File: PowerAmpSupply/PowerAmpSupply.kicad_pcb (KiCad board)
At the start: 2 copper layers, 52 parts, among them Q1 GAN3R2-100CBE, Q2 PNP, Q3 GAN3R2-100CBE, Q4 PNP, U1 LM5123-Q1

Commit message: CleanLVSupply reduce -17V switch frequency
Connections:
- net Net-(Q2-C) renamed /SW
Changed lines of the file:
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@@
 	(net 23 "Net-(U1-RT)")
 	(net 24 "/PGOOD")
-	(net 25 "Net-(Q2-C)")
+	(net 25 "/SW")
 	(footprint "Capacitor_SMD:C_0805_2012Metric"
 		(layer "F.Cu")
@@
 			(size 0.24 0.7)
 			(layers "F.Cu" "F.Paste" "F.Mask")
-			(net 25 "Net-(Q2-C)")
+			(net 25 "/SW")
 			(pinfunction "SW")
 			(pintype "passive")
@@
 			(size 1.5 1.5)
 			(layers "F.Cu" "F.Mask")
-			(net 25 "Net-(Q2-C)")
+			(net 25 "/SW")
 			(pinfunction "1")
 			(pintype "passive")
@@
 			(layers "F.Cu" "F.Paste" "F.Mask")
 			(roundrect_rratio 0.25)
-			(net 25 "Net-(Q2-C)")
+			(net 25 "/SW")
 			(pinfunction "S")
 			(pintype "passive")
@@
 			(layers "F.Cu" "F.Paste" "F.Mask")
 			(roundrect_rratio 0.25)
-			(net 25 "Net-(Q2-C)")
+			(net 25 "/SW")
 			(pinfunction "S")
 			(pintype "passive")
@@
 			(layers "F.Cu" "F.Paste" "F.Mask")
 			(roundrect_rratio 0.25)
-			(net 25 "Net-(Q2-C)")
+			(net 25 "/SW")
 			(pinfunction "S")
 			(pintype "passive")
@@
 			(layers "F.Cu" "F.Paste" "F.Mask")
 			(roundrect_rratio 0.25)
-			(net 25 "Net-(Q2-C)")
+			(net 25 "/SW")
 			(pinfunction "S")
 			(pintype "passive")
@@
 			(layers "F.Cu" "F.Paste" "F.Mask")
 			(roundrect_rratio 0.25)
-			(net 25 "Net-(Q2-C)")
+			(net 25 "/SW")
 			(pintype "passive")
 		)
@@
 			(layers "F.Cu" "F.Paste" "F.Mask")
 			(roundrect_rratio 0.25)
-			(net 25 "Net-(Q2-C)")
+			(net 25 "/SW")
 			(pinfunction "D")
 			(pintype "passive")
@@
 			(layers "F.Cu" "F.Paste" "F.Mask")
 			(roundrect_rratio 0.25)
-			(net 25 "Net-(Q2-C)")
+			(net 25 "/SW")
 			(pinfunction "D")
 			(pintype "passive")
@@
 			(layers "F.Cu" "F.Paste" "F.Mask")
 			(roundrect_rratio 0.25)
-			(net 25 "Net-(Q2-C)")
+			(net 25 "/SW")
 			(pinfunction "D")
 			(pintype "passive")
@@
 			(layers "F.Cu" "F.Paste" "F.Mask")
 			(roundrect_rratio 0.25)
-			(net 25 "Net-(Q2-C)")
+			(net 25 "/SW")
 			(pinfunction "2")
 			(pintype "passive")
@@
 			(layers "F.Cu" "F.Paste" "F.Mask")
 			(roundrect_rratio 0.25)
-			(net 25 "Net-(Q2-C)")
+			(net 25 "/SW")
 			(pinfunction "C")
 			(pintype "passive")
@@
 			(layers "F.Cu" "F.Paste" "F.Mask")
 			(roundrect_rratio 0.25)
-			(net 25 "Net-(Q2-C)")
+			(net 25 "/SW")
 			(pinfunction "A")
 			(pintype "passive")
@@
 			(layers "F.Cu" "F.Paste" "F.Mask")
 			(roundrect_rratio 0.25)
-			(net 25 "Net-(Q2-C)")
+			(net 25 "/SW")
 			(pinfunction "A")
 			(pintype "passive")

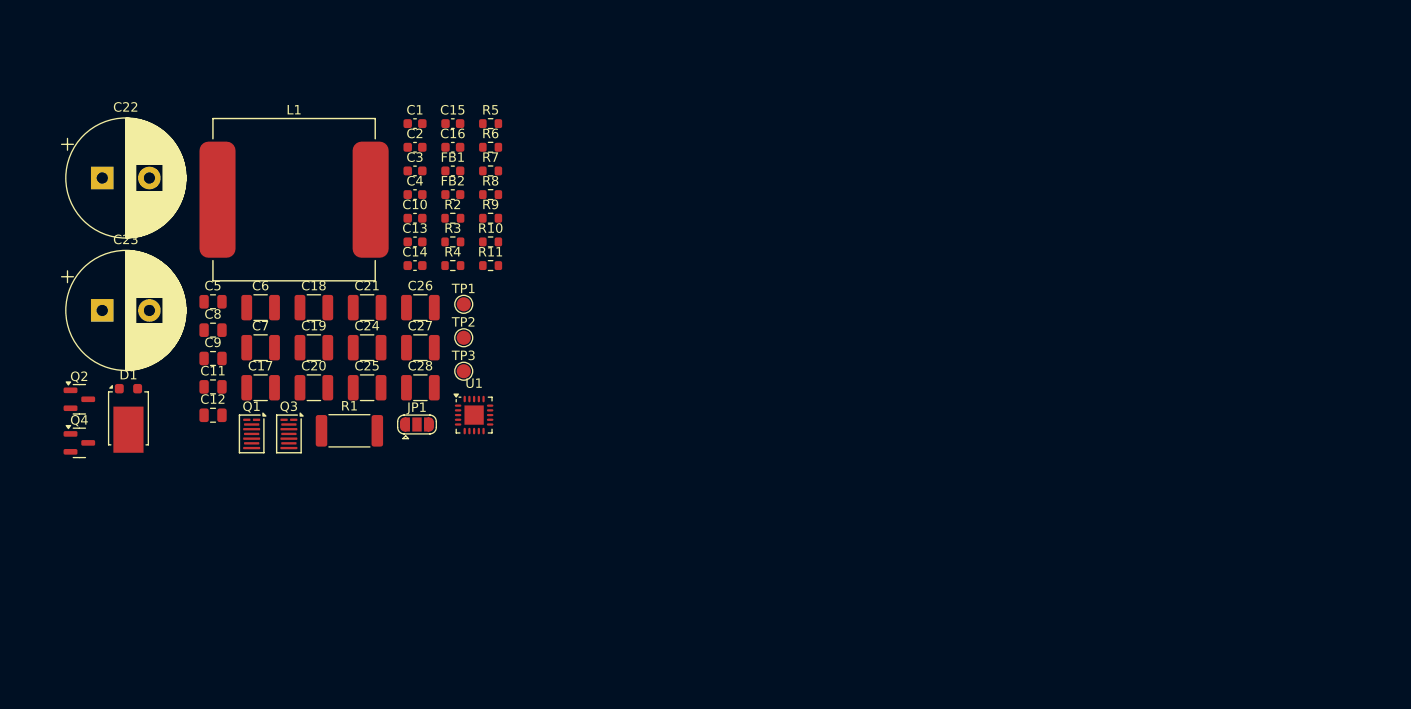
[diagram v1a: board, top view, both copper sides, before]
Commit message: PowerAmplifier initially complete, PowerAmpSupply progress
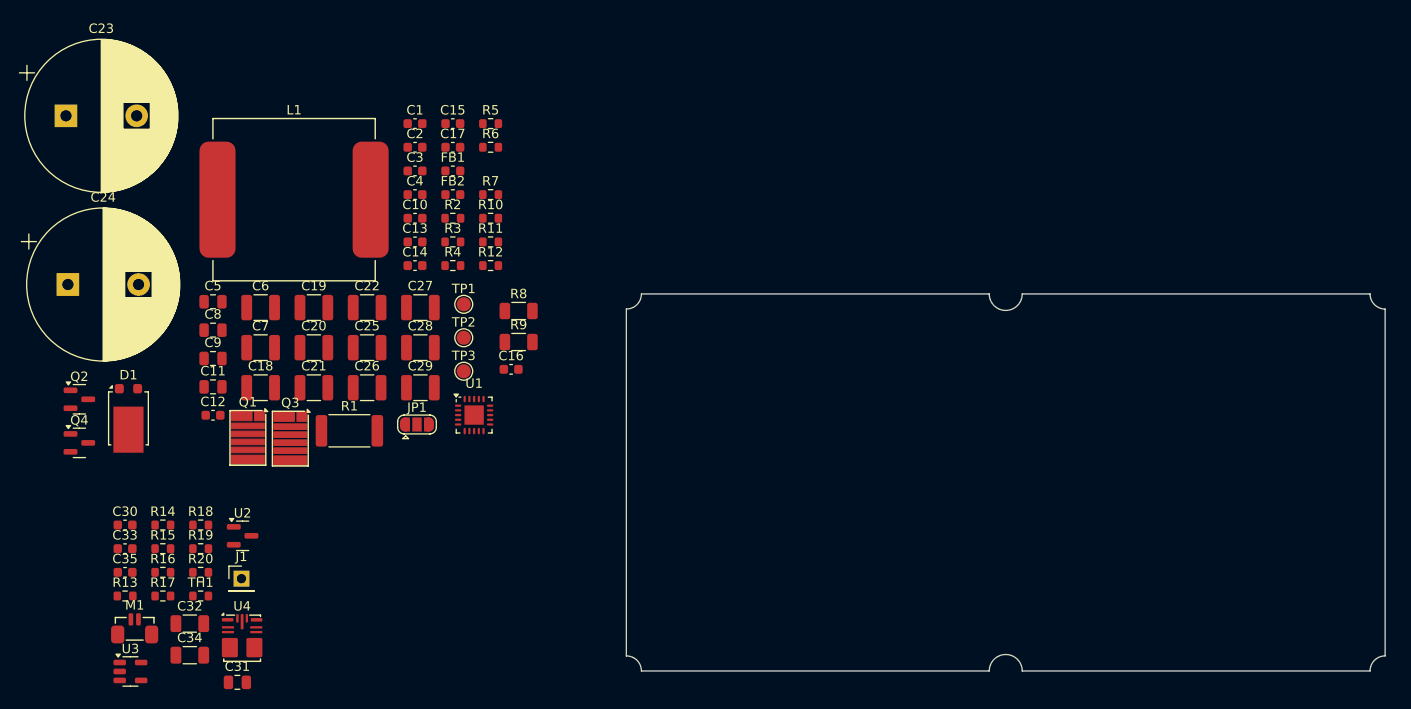
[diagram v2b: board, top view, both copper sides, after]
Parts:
- removed the R7 at (95.3, 67.0)
- added C16: ?pF 100+V, Capacitor_SMD:C_0603_1608Metric, F.Cu at (97.5, 88.0)
- added C30: 22pF, Capacitor_SMD:C_0603_1608Metric, F.Cu at (56.6, 104.5)
- added C31: 10µF 25V, Capacitor_SMD:C_0805_2012Metric, F.Cu at (68.5, 121.2)
- added C32: 2.2µF 100Vl, Capacitor_SMD:C_1206_3216Metric, F.Cu at (63.4, 115.0)
- added C33: 0.1µF 100V, Capacitor_SMD:C_0603_1608Metric, F.Cu at (56.6, 107.0)
- added C34: 10µF 50V, Capacitor_SMD:C_1206_3216Metric, F.Cu at (63.4, 118.3)
- added C35: 0.1µF, Capacitor_SMD:C_0603_1608Metric, F.Cu at (56.6, 109.5)
- added J1: VTRK_EXT, Connector_PinHeader_2.54mm:PinHeader_1x01_P2.54mm_Vertical, F.Cu at (68.9, 110.2)
- added M1: 12V 6Vstart <100mA, BW_Connectors:Amphenol_MINITEK_0.8_2P_V, F.Cu at (57.6, 115.5)
- added R13: 28kΩ 0.1%, Resistor_SMD:R_0603_1608Metric, F.Cu at (56.6, 112.0)
- added R14: 28kΩ 0.1%, Resistor_SMD:R_0603_1608Metric, F.Cu at (60.6, 104.5)
- added R15: 10.5kΩ 0.1%, Resistor_SMD:R_0603_1608Metric, F.Cu at (60.6, 107.0)
- added R16: 110kΩ, Resistor_SMD:R_0603_1608Metric, F.Cu at (60.6, 109.5)
- added R17: 13kΩ, Resistor_SMD:R_0603_1608Metric, F.Cu at (60.6, 112.0)
- added R18: 10kΩ, Resistor_SMD:R_0603_1608Metric, F.Cu at (64.6, 104.5)
- added R19: 0Ω, Resistor_SMD:R_0603_1608Metric, F.Cu at (64.6, 107.0)
- added R20: 0Ω, Resistor_SMD:R_0603_1608Metric, F.Cu at (64.6, 109.5)
- added R8: ?Ω, Resistor_SMD:R_1206_3216Metric, F.Cu at (98.3, 81.8)
- added R9: ?Ω, Resistor_SMD:R_1206_3216Metric, F.Cu at (98.3, 85.1)
- added TH1: 10kΩ 3950B, Resistor_SMD:R_0603_1608Metric, F.Cu at (64.6, 112.0)
- added U2: NCP51460, Package_TO_SOT_SMD:SOT-23, F.Cu at (69.0, 105.7)
- added U3: AP2202-ADJ, Package_TO_SOT_SMD:SOT-23-5, F.Cu at (57.1, 120.0)
- added U4: TPSM365R3, BW_Active:TI_QFN-FCMOD-HR, F.Cu at (69.0, 116.5)
- C11: value 4.7µF -> 4.7µF 25Vl
- C12: value 10µF -> 4.7µF; footprint Capacitor_SMD:C_0805_2012Metric -> Capacitor_SMD:C_0603_1608Metric
- C23: renamed from C22; value 560µF 63V -> 1mF 80V; footprint Capacitor_THT:CP_Radial_D12.5mm_P5.00mm -> Capacitor_THT:CP_Radial_D16.0mm_P7.50mm
- C24: renamed from C23; value 560µF 63V -> 1mF 80V; footprint Capacitor_THT:CP_Radial_D12.5mm_P5.00mm -> Capacitor_THT:CP_Radial_D16.0mm_P7.50mm
- Q1, Q3: value GAN3R2-100CBE -> EPC2306; footprint BW_Active:WLCSP-8-SOT8072 -> BW_Active:EPC2306
- R6: value 3.3Ω -> 1Ω
- R7: renamed from R8; value 3.3Ω -> 1Ω
- moved C23 7.64 mm to (50.3, 61.1)
- moved C24 4.57 mm to (50.5, 79.0)
- moved Q1 0.58 mm to (69.6, 95.3)
- moved Q3 0.52 mm to (74.1, 95.3)
- renumbered C16 to C17, C17 to C18, C18 to C19, C19 to C20, C20 to C21, C21 to C22, C24 to C25, C25 to C26, C26 to C27, C27 to C28, C28 to C29, R9 to R10, R10 to R11, R11 to R12
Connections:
- net Net-(C2-Pad1) renamed /EN
- C12 pad 1: Net-(U1-TRK) -> /VTRK
- U1 pad 18: Net-(U1-TRK) -> /VTRK
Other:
- board outline added: 80.5 x 40 mm
- copper layers 2 -> 4

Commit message: PowerAmpSupply FET change and layout progress
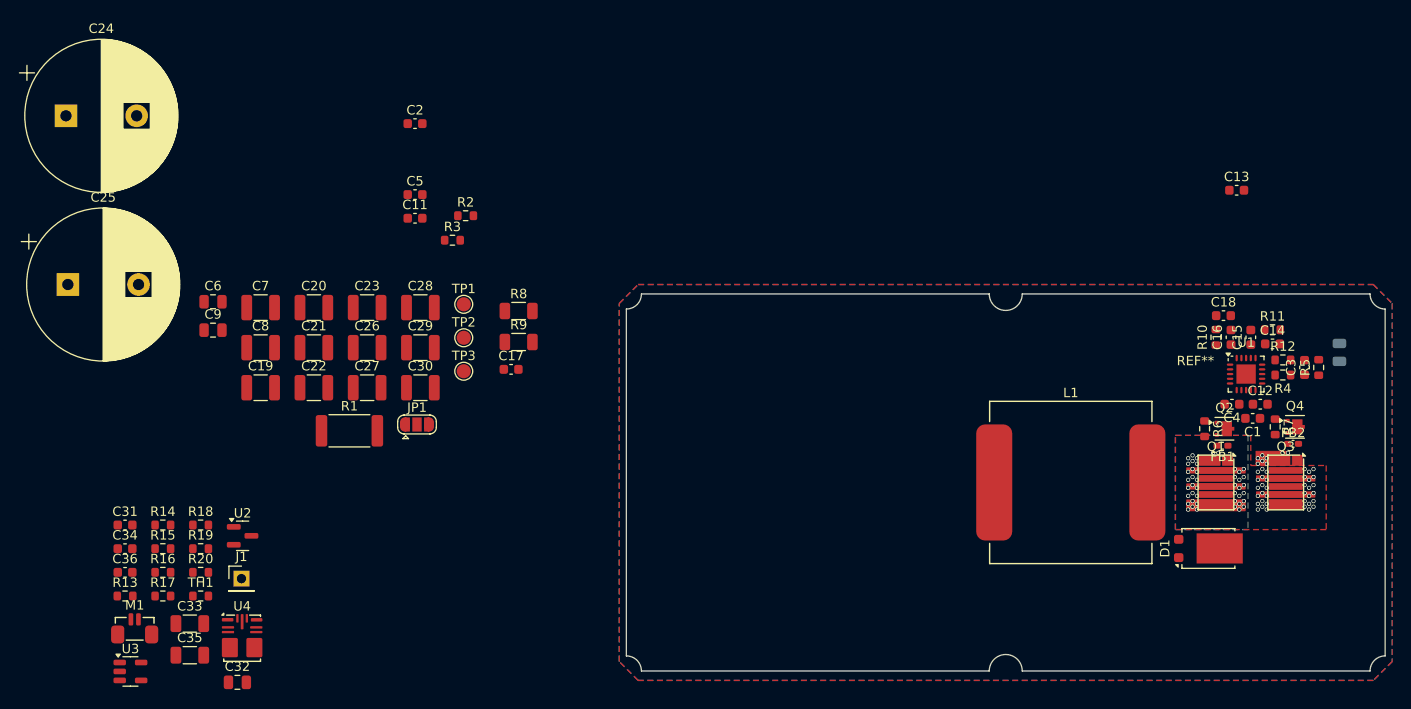
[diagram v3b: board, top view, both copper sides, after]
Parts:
- added C1: 0.1µF, Capacitor_SMD:C_0603_1608Metric, F.Cu at (176.2, 93.2)
- added REF**: ATS-xPX035035035_NoMounts, BW_PassiveMechanical:ATS-xPX035035035_NoMounts, F.Cu at (170.1, 100.0)
- C10: renamed from C9; moved to B.Cu
- C12: renamed from C11; value 4.7µF 25Vl -> 4.7µF; footprint Capacitor_SMD:C_0805_2012Metric -> Capacitor_SMD:C_0603_1608Metric
- FB1, FB2: footprint Inductor_SMD:L_0603_1608Metric -> Inductor_SMD:L_0402_1005Metric_Pad0.77x0.64mm_HandSolder
- Q2, Q4: footprint Package_TO_SOT_SMD:SOT-23 -> Package_SON:HUSON-3-1EP_2x2mm_P1.3mm_EP1.1x1.6mm
- moved Q4 129.0 mm to (180.7, 94.1)
- moved Q2 121.5 mm to (173.2, 94.3)
- moved C10 119.5 mm to (185.4, 86.2), turned to 90 degrees
- moved D1 115.4 mm to (171.5, 107.0), turned to 90 degrees
- moved C13 111.2 mm to (174.5, 69.0)
- moved C12 111.1 mm to (177.0, 91.7)
- moved Q3 105.7 mm to (179.7, 100.0)
- moved Q1 102.8 mm to (172.3, 100.0)
- moved C3 97.2 mm to (181.7, 87.8), turned to 90 degrees
- moved FB2 93.0 mm to (180.5, 95.9)
- moved C14 91.6 mm to (178.3, 85.3)
- moved R5 91.6 mm to (183.2, 87.8), turned to 90 degrees
- moved C4 90.1 mm to (174.0, 91.7), turned to 180 degrees
- moved C15 89.0 mm to (176.0, 84.6), turned to 90 degrees
- moved R4 88.8 mm to (179.4, 88.6), turned to 180 degrees
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- renumbered C10 to C11, C12 to C13, C13 to C14, C14 to C15, C15 to C16, C16 to C17, C17 to C18, C18 to C19, C1 to C2, C19 to C20, C20 to C21, C21 to C22, C22 to C23, C23 to C24, C24 to C25, C25 to C26, C26 to C27, C27 to C28, C28 to C29, C2 to C3, C29 to C30, C30 to C31, C31 to C32, C32 to C33, C33 to C34, C34 to C35, C35 to C36, C3 to C4, C4 to C5, C5 to C6, C6 to C7, C7 to C8, C8 to C9
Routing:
- net GND: vias 0 -> 20
- net /VOUT: vias 0 -> 24
- net /SW: vias 0 -> 44
- added copper zone on F.Cu, net /SW
- added copper zone on In1.Cu, net /SW
- added copper zone on In2.Cu, net /SW
- added copper zone on B.Cu, net /VOUT
- added copper zone on In2.Cu, net /VOUT
- added copper zone on B.Cu, net GND
- added copper zone on F.Cu, net GND
- added copper zone on In1.Cu, net GND
- added copper zone on In2.Cu, net GND

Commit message: PowerAmpSupply almost done
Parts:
- added C25: 10µF 100V x2, Capacitor_SMD:C_1210_3225Metric, B.Cu at (154.8, 100.1)
- added C28: 1mF 80V, Capacitor_THT:CP_Radial_D16.0mm_P7.50mm, F.Cu at (125.5, 107.4)
- added C34: 10µF 100V x2, Capacitor_SMD:C_1210_3225Metric, B.Cu at (157.0, 114.4)
- added C7: 1mF 35V, Capacitor_THT:CP_Radial_D10.0mm_P5.00mm, F.Cu at (145.4, 88.0)
- added J1: VIN_BRIDGE, BW_PassiveMechanical:HolePad_2.5mm_3.5mm, F.Cu at (116.4, 82.6)
- added J2: VIN_BRIDGE, BW_PassiveMechanical:HolePad_2.5mm_3.5mm, F.Cu at (159.5, 85.3)
- added J3: GND_BRIDGE, BW_PassiveMechanical:HolePad_2.5mm_3.5mm, F.Cu at (122.8, 94.0)
- added J4: GND_BRIDGE, BW_PassiveMechanical:HolePad_2.5mm_3.5mm, F.Cu at (177.8, 100.3)
- added J5: VOUT, BW_Connectors:TE_644749-2, F.Cu at (113.4, 108.3)
- added J6: VIN, BW_Connectors:TE_2042274_Solder, F.Cu at (115.5, 93.7)
- added R1: 3mΩ 2W, Resistor_SMD:R_0612_1632Metric, F.Cu at (161.5, 89.8)
- added REF**: MountingHole_2.2mm_M2, MountingHole:MountingHole_2.2mm_M2, B.Cu at (171.0, 96.3)
- added REF**: MountingHole_2.2mm_M2, MountingHole:MountingHole_2.2mm_M2, B.Cu at (184.4, 112.6)
- C10: renamed from C9; moved to B.Cu
- C14: renamed from C13; moved to B.Cu
- C20: renamed from C19; moved to B.Cu
- C21: renamed from C20; moved to B.Cu
- C22: renamed from C21; moved to B.Cu
- C23: renamed from C22; moved to B.Cu
- C24: renamed from C23; moved to B.Cu
- C29: renamed from C26; moved to B.Cu
- C30: renamed from C27; moved to B.Cu
- C31: renamed from C28; moved to B.Cu
- C32: renamed from C29; moved to B.Cu
- C33: renamed from C30; moved to B.Cu
- C36: renamed from C32; moved to B.Cu
- C5, C6, JP1, TP1, TP2, TP3, U2, U3: moved to B.Cu
- C8: renamed from C7; moved to B.Cu
- C9: renamed from C8; moved to B.Cu
- M1: footprint BW_Connectors:Amphenol_MINITEK_0.8_2P_V -> BW_Connectors:Amphenol_MINITEK_0.8_2P_V_BoardEdge
- R14: renamed from R13; moved to B.Cu
- R15: renamed from R14; moved to B.Cu
- R16: renamed from R15; moved to B.Cu
- R18: renamed from R17; value 13kΩ -> 23.2kΩ; moved to B.Cu
- R2: renamed from R1; value 1.5mΩ 3W -> 3mΩ 2W; footprint Resistor_SMD:R_2512_6332Metric -> Resistor_SMD:R_0612_1632Metric
- R20: renamed from R19; moved to B.Cu
- R21: renamed from R20; moved to B.Cu
- TH1: value 10kΩ 3950B -> 10kΩ 4250B; footprint Resistor_SMD:R_0603_1608Metric -> Resistor_SMD:R_0402_1005Metric_Pad0.72x0.64mm_HandSolder
- moved M1 127.0 mm to (179.9, 81.2), turned to 180 degrees
- moved U3 125.5 mm to (177.1, 83.1)
- moved R18 122.7 mm to (180.4, 85.6), turned to 180 degrees
- moved R21 121.0 mm to (182.6, 83.0), turned to -90 degrees
- moved R14 118.8 mm to (173.4, 90.4), turned to -90 degrees
- moved C36 118.6 mm to (180.8, 83.1), turned to 90 degrees
- moved C39 117.6 mm to (175.5, 82.6), turned to 90 degrees
- moved TH1 116.1 mm to (180.2, 101.0), turned to 180 degrees
- moved R16 115.5 mm to (174.9, 90.4), turned to 90 degrees
- moved C38 115.3 mm to (169.9, 85.6), turned to 180 degrees
- moved R20 114.8 mm to (177.4, 85.6), turned to 180 degrees
- moved C6 114.5 mm to (176.9, 109.1)
- moved C40 114.4 mm to (167.4, 81.0), turned to 180 degrees
- moved R15 112.2 mm to (171.9, 90.4), turned to -90 degrees
- moved C35 112.1 mm to (166.6, 83.3), turned to -90 degrees
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- renumbered C10 to C11, C11 to C13, C14 to C15, C15 to C16, C16 to C17, C17 to C18, C18 to C19, C24 to C26, C25 to C27, C4 to C3, C31 to C35, C33 to C37, C34 to C38, C35 to C39, C3 to C4, C36 to C40, J1 to J7, R9 to R10, R10 to R11, R11 to R12, R12 to R13, R16 to R17, R18 to R19, R2 to R3, R3 to R4, R4 to R5, R5 to R6, R6 to R7, R7 to R8, R8 to R9
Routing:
- net /VIN: track 0.00 -> 76.3 mm, vias 0 -> 1
- net /VOUT: track 0.00 -> 76.3 mm, vias 24 -> 26
- net Net-(J7-Pin_1): track 0.00 -> 33.7 mm
- net Net-(U1-CSN): track 0.00 -> 6.97 mm
- net Net-(Q2-B): track 0.00 -> 6.94 mm
- net Net-(JP1-B): track 0.00 -> 5.33 mm, vias 0 -> 2
- net Net-(U4-FB/BIAS): track 0.00 -> 5.21 mm
- net +12V: track 0.00 -> 4.46 mm
- net Net-(L1-Pad1): track 0.00 -> 4.35 mm
- net /SW: track 0.00 -> 2.66 mm, vias 44 -> 54
- net GND: track 0.00 -> 2.10 mm, vias 20 -> 22
- net Net-(U4-VCC): track 0.00 -> 1.49 mm
- added copper zone on B.Cu, net /VIN
- added copper zone on F.Cu, net /VIN
